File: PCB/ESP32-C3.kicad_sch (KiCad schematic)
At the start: 41 parts, among them J1 BattConn+, J2 BattConn-, SW1 TAK_6mm_THT, U1 USB-C-16P-SMD, U2 XT4052K421MR-G, U3 ESP32-C3, U4 RS3236-3.3YF5, X1 DPS_I2C, Y1 40MHz_S3240000151040

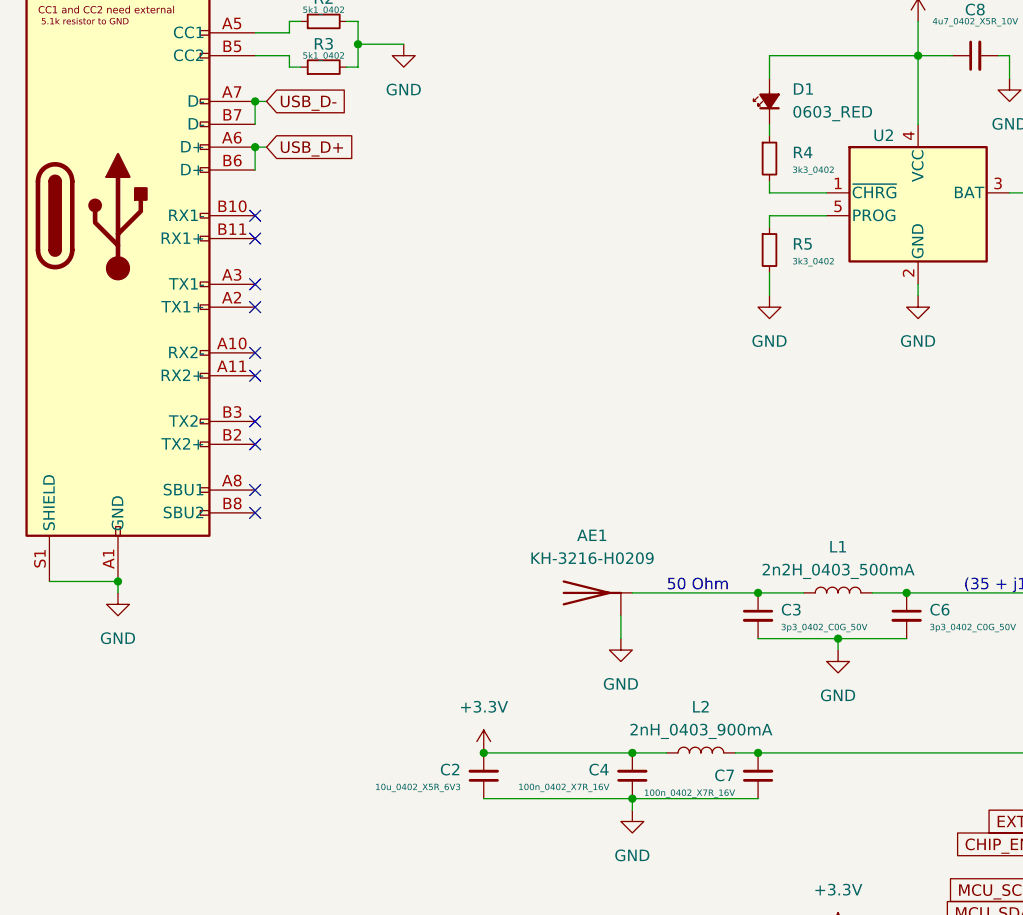
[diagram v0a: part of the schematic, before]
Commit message: update to KiCad 7
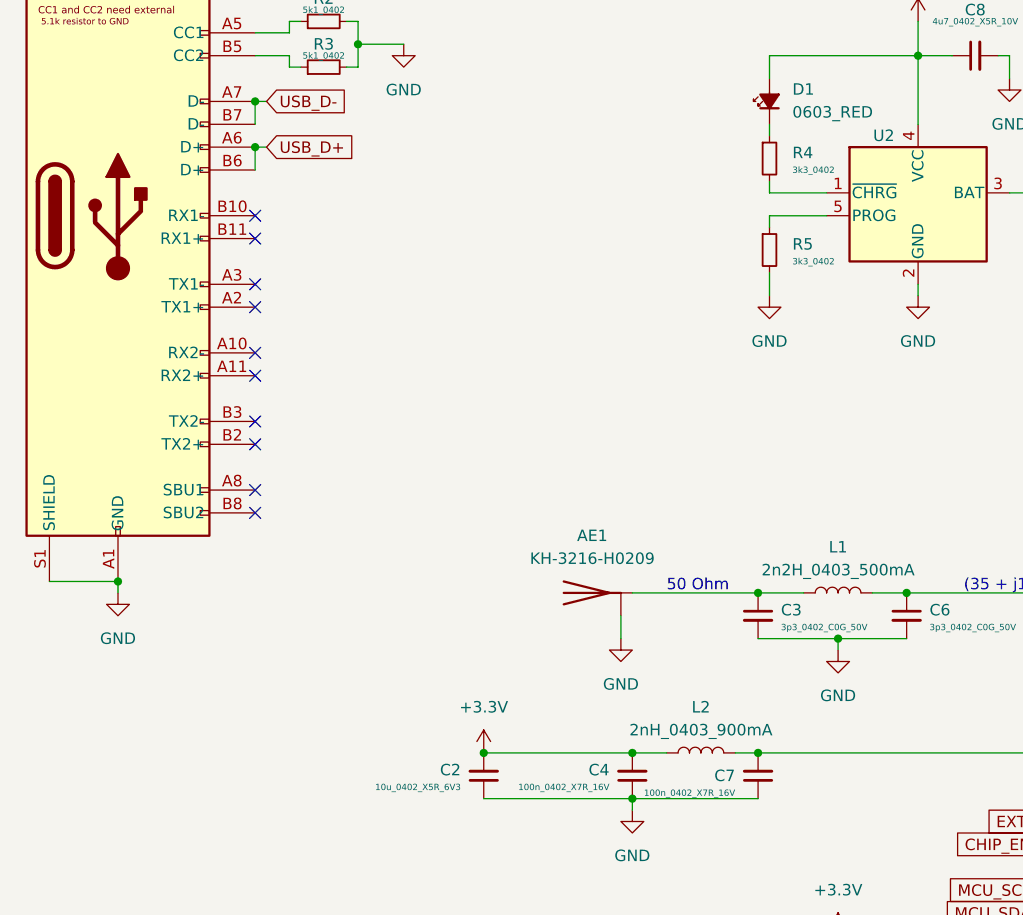
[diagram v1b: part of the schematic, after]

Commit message: updated the charging circuit
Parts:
- removed C10, C18: 1u_0402_X5R_25V, Capacitor_SMD:C_0402_1005Metric, symbol capacitor_smd_standard:1u_0402_X5R_25V
- removed C13: 10n_0402_X7R_50V, Capacitor_SMD:C_0402_1005Metric, symbol capacitor_smd_standard:10n_0402_X7R_50V
- removed C8: 4u7_0402_X5R_10V, Capacitor_SMD:C_0402_1005Metric, symbol ESP32-C3_Bib:4u7_0402_X5R_10V
- removed C9: 10u_0402_X5R_6V3, Capacitor_SMD:C_0402_1005Metric, symbol capacitor_smd_standard:10u_0402_X5R_6V3
- removed D1: 0603_RED, LED_SMD:LED_0603_1608Metric, symbol led:0603_RED
- removed D2, D3: 1N5819WS(Basic), Diode_SMD:D_SOD-323_HandSoldering, symbol 1_diodes:1N5819WS(Basic)
- removed J1: BattConn+, Connector_PinSocket_2.54mm:PinSocket_1x01_P2.54mm_Vertical, symbol Connector_Generic:Conn_01x01
- removed J2: BattConn-, Connector_PinSocket_2.54mm:PinSocket_1x01_P2.54mm_Vertical, symbol Connector_Generic:Conn_01x01
- removed R4, R5: 3k3_0402, Resistor_SMD:R_0402_1005Metric, symbol resistor_smd_standard:3k3_0402
- removed SW1: TAK_6mm_THT, Button_Switch_THT:SW_PUSH_6mm_H5mm, symbol 1_switch:TAK_6mm_THT
- removed U2: XT4052K421MR-G, Package_TO_SOT_SMD:TSOT-23-5, symbol ESP32-C3_Bib:XT4052K421MR-G
- removed U4: RS3236-3.3YF5, Package_TO_SOT_SMD:SOT-23-5, symbol ESP32-C3_Bib:RS3236-3.3YF5
- added SW2: TS4535TP 250gf 009, switch:SW_SPST_TL3305B, symbol 1_switch:TS4535TP 250gf 009
- added TP1: BAT+, testpoints:TP3, symbol 0_testpoints:TP_3CH
- added TP2: BAT-, testpoints:TP3, symbol 0_testpoints:TP_3CH
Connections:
- net +BATT: now also TP1.1
- net EXTI: now also SW2.2
- net GND: now also SW2.1, TP2.1
- net GPIO8: now reaches U3.14 (GPIO8)
- no-connect marks 27 -> 26
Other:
- added sheet charger (charger.kicad_sch)
- note removed: "Charching Current: V_prog = 1V, R_prog=3.3k 303mA = (V_prog / R_prog) * 1000"

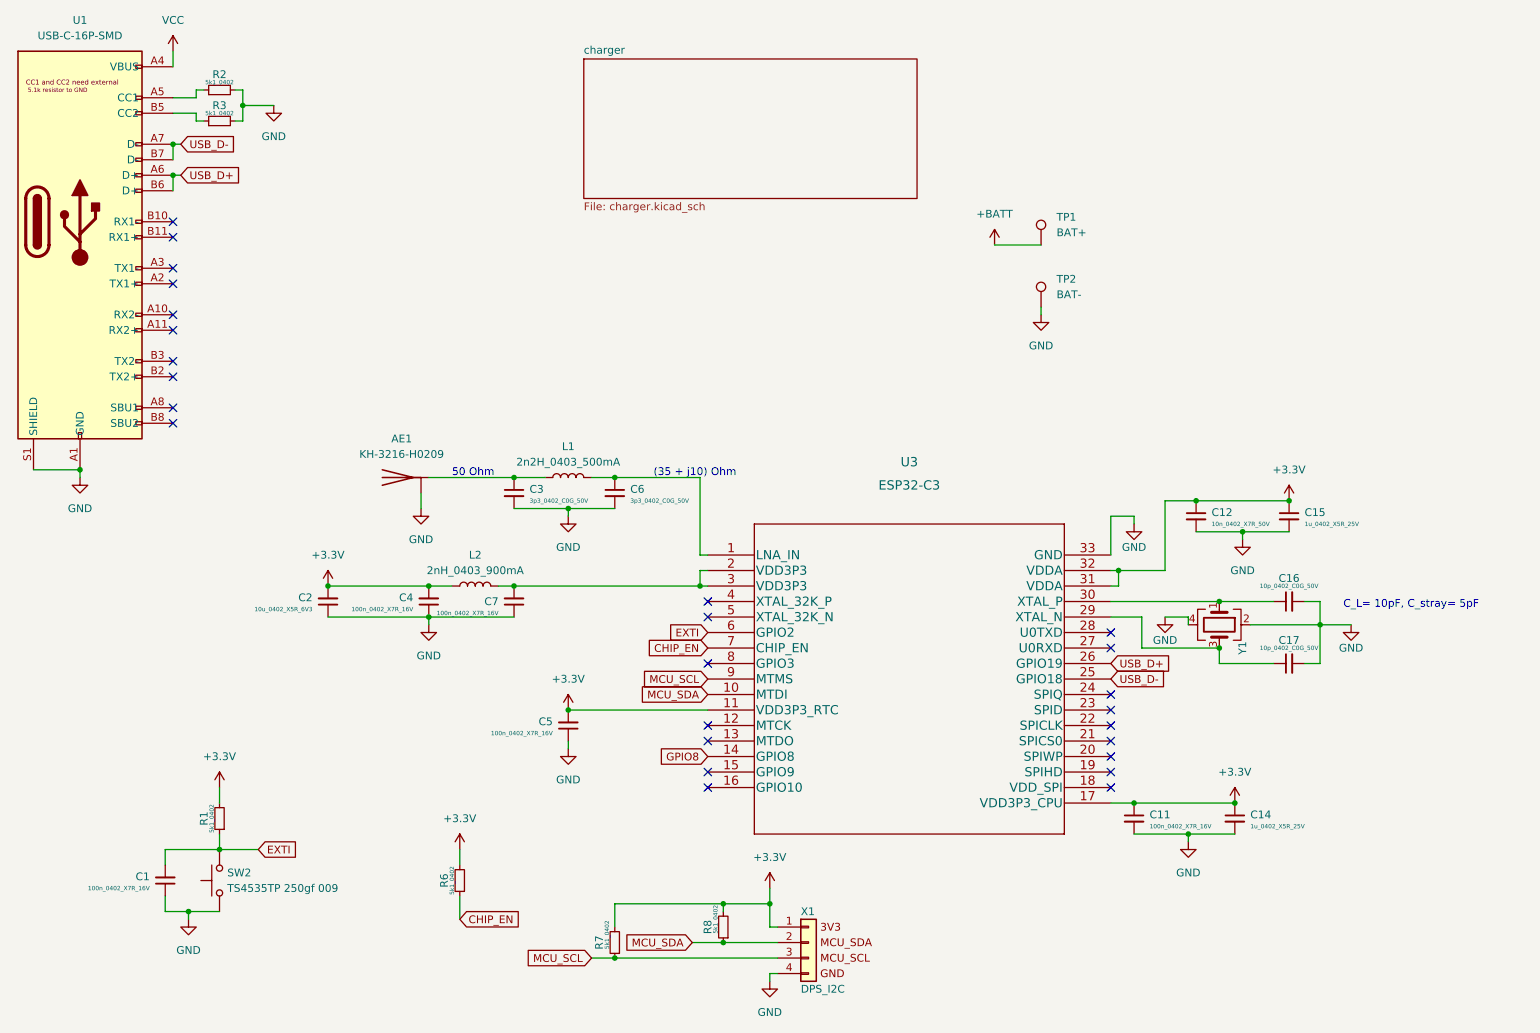
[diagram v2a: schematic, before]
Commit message: Mit dem Layout angefangen
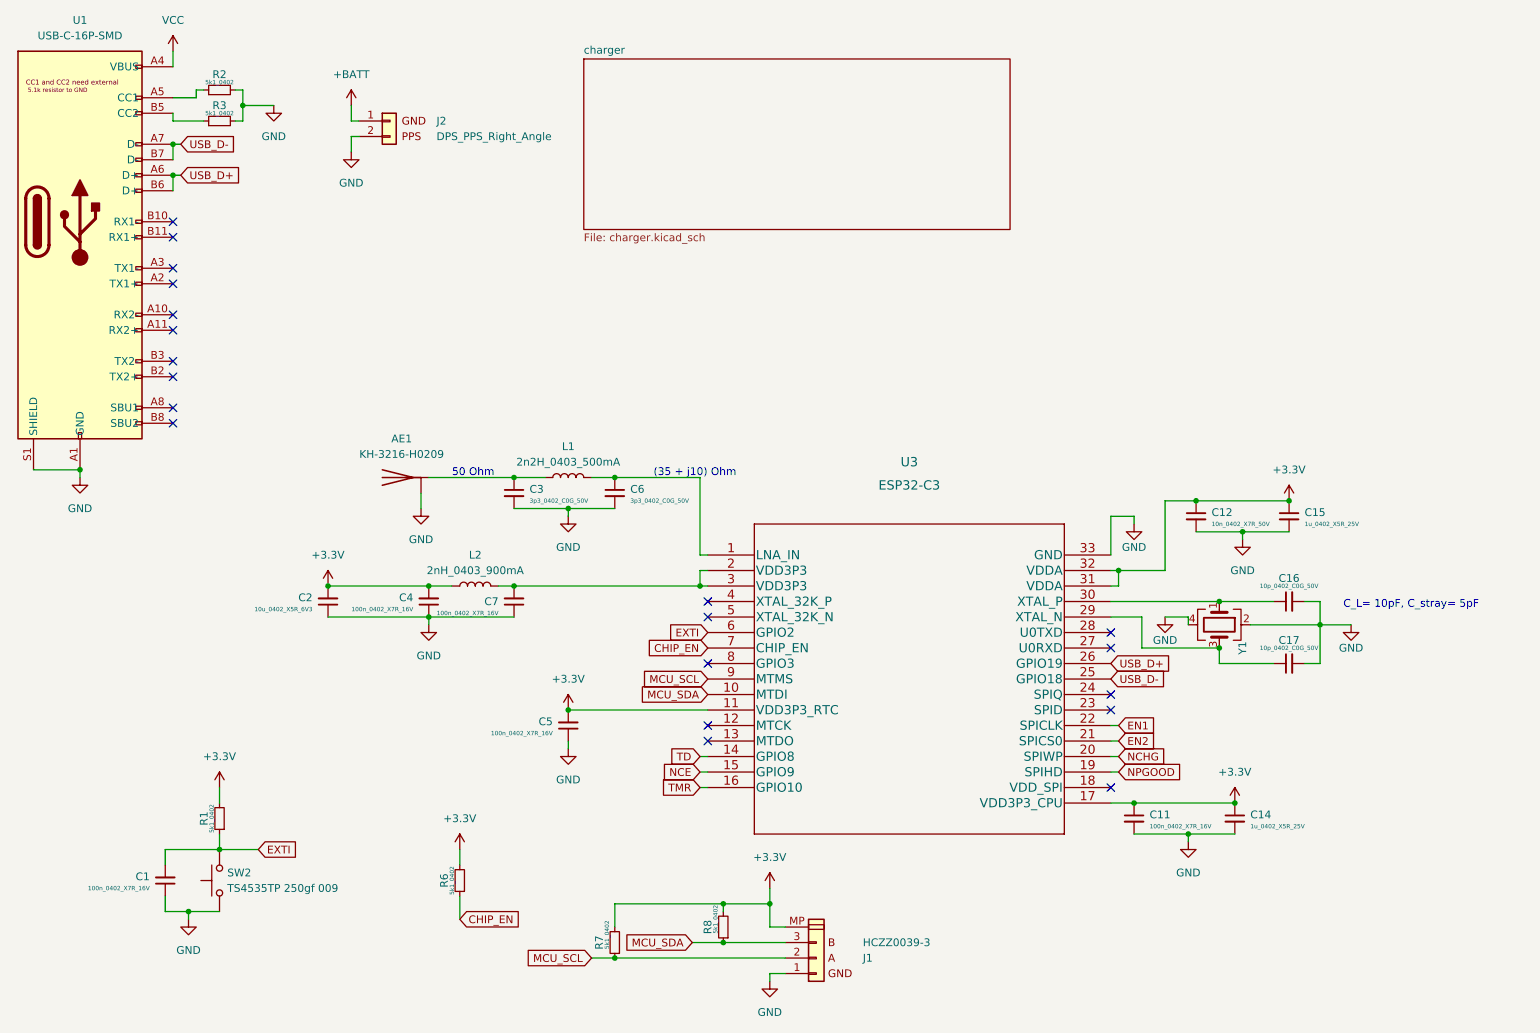
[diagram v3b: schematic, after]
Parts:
- removed TP1: BAT+, testpoints:TP3, symbol 0_testpoints:TP_3CH
- removed TP2: BAT-, testpoints:TP3, symbol 0_testpoints:TP_3CH
- removed X1: DPS_I2C, Connector_JST:JST_PH_B4B-PH-K_1x04_P2.00mm_Vertical, symbol DPS_connectors:DPS_I2C
- added J1: HCZZ0039-3, Connector_JST:JST_SH_SM03B-SRSS-TB_1x03-1MP_P1.00mm_Horizontal, symbol DPS_connectors:DPS_485
- added J2: DPS_PPS_Right_Angle, Connector_JST:JST_PH_S2B-PH-K_1x02_P2.00mm_Horizontal, symbol DPS_connectors:DPS_PPS_Right_Angle
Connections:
- net +3.3V: now also J1.MP
- net +BATT: now also J2.1 (Pin_1)
- net GND: now also J1.1 (Pin_1), J2.2 (Pin_2)
- net MCU_SCL: now also J1.2 (Pin_2)
- net MCU_SDA: now also J1.3 (Pin_3)
- net NCE: now reaches U3.15 (GPIO9)
- net TMR: now reaches U3.16 (GPIO10)
- net NPGOOD: now reaches U3.19 (SPIHD)
- net NCHG: now reaches U3.20 (SPIWP)
- net EN2: now reaches U3.21 (SPICS0)
- net EN1: now reaches U3.22 (SPICLK)
- net GPIO8 renamed TD
- no-connect marks 26 -> 20

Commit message: Layout weiter gemacht.
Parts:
- C1, C11, C4, C5, C7: QtyReel (none) -> 10000
- U1: Partnumber (none) -> SOFNG MC-311D
- U3: footprint ESP32-C3:ESP32-C3 -> Package_DFN_QFN:QFN-32-1EP_5x5mm_P0.5mm_EP3.7x3.7mm
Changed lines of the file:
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@@
       (effects (font (size 1.27 1.27)))
     )
-    (property "Value" "10p_0402_C0G_50V" (at 228.6 110.49 90)
-      (effects (font (size 0.7 0.7)))
+    (property "Value" "10p_0402_C0G_50V" (at 230.632 112.776 0)
+      (effects (font (size 0.7 0.7)) (justify left))
     )
     (property "Footprint" "Capacitor_SMD:C_0402_1005Metric" (at 228.6 113.03 0)
@@
   (symbol (lib_id "capacitor_smd_standard:100n_0402_X7R_16V") (at 87.63 113.03 0) (mirror x) (unit 1)
     (in_bom yes) (on_board yes) (dnp no) (fields_autoplaced)
-    (property "Reference" "C4" (at 85.09 112.3885 0)
+    (property "Reference" "C4" (at 85.09 112.3886 0)
       (effects (font (size 1.27 1.27)) (justify right))
     )
@@
       (effects (font (size 1.27 1.27)) hide)
     )
+    (property "QtyReel" "10000" (at 87.63 113.03 0)
+      (effects (font (size 1.27 1.27)) hide)
+    )
     (pin "1")
     (pin "2")
@@
   (symbol (lib_id "capacitor_smd_standard:10u_0402_X5R_6V3") (at 71.12 113.03 0) (mirror x) (unit 1)
     (in_bom yes) (on_board yes) (dnp no) (fields_autoplaced)
-    (property "Reference" "C2" (at 68.58 112.3885 0)
+    (property "Reference" "C2" (at 68.58 112.3886 0)
       (effects (font (size 1.27 1.27)) (justify right))
     )
@@
       (effects (font (size 1.27 1.27)))
     )
-    (property "Value" "5k1_0402" (at 116.84 167.64 90)
-      (effects (font (size 0.7 0.7)))
+    (property "Value" "5k1_0402" (at 116.84 168.91 0)
+      (effects (font (size 0.7 0.7)) (justify left))
     )
     (property "Footprint" "Resistor_SMD:R_0402_1005Metric" (at 134.62 157.48 0)
@@
   (symbol (lib_id "capacitor_smd_standard:1u_0402_X5R_25V") (at 219.71 148.59 0) (unit 1)
     (in_bom yes) (on_board yes) (dnp no) (fields_autoplaced)
-    (property "Reference" "C14" (at 222.25 147.9612 0)
+    (property "Reference" "C14" (at 222.25 147.9613 0)
       (effects (font (size 1.27 1.27)) (justify left))
     )
@@
       (effects (font (size 1.27 1.27)))
     )
-    (property "Value" "2nH_0403_900mA" (at 95.25 107.95 90)
+    (property "Value" "2nH_0403_900mA" (at 95.25 108.585 90)
       (effects (font (size 1.27 1.27)))
     )
@@
       (effects (font (size 1.27 1.27)))
     )
-    (property "Value" "2n2H_0403_500mA" (at 110.49 90.17 90)
+    (property "Value" "2n2H_0403_500mA" (at 110.49 90.805 90)
       (effects (font (size 1.27 1.27)))
     )
@@
       (effects (font (size 1.27 1.27)))
     )
-    (property "Value" "5k1_0402" (at 134.62 165.1 90)
-      (effects (font (size 0.7 0.7)))
+    (property "Value" "5k1_0402" (at 134.62 166.37 0)
+      (effects (font (size 0.7 0.7)) (justify left))
     )
     (property "Footprint" "Resistor_SMD:R_0402_1005Metric" (at 152.4 154.94 0)
@@
       (effects (font (size 1.27 1.27)))
     )
-    (property "Value" "10p_0402_C0G_50V" (at 228.6 120.65 90)
-      (effects (font (size 0.7 0.7)))
+    (property "Value" "10p_0402_C0G_50V" (at 230.632 122.936 0)
+      (effects (font (size 0.7 0.7)) (justify left))
     )
     (property "Footprint" "Capacitor_SMD:C_0402_1005Metric" (at 228.6 123.19 0)
@@
       (effects (font (size 1.27 1.27)))
     )
-    (property "Value" "5k1_0402" (at 53.34 33.02 90)
-      (effects (font (size 0.7 0.7)))
+    (property "Value" "5k1_0402" (at 53.34 33.02 0)
+      (effects (font (size 0.7 0.7)) (justify left))
     )
     (property "Footprint" "Resistor_SMD:R_0402_1005Metric" (at 64.77 50.8 0)
@@
       (effects (font (size 1.27 1.27)))
     )
-    (property "Value" "5k1_0402" (at 91.44 158.75 90)
-      (effects (font (size 0.7 0.7)))
+    (property "Value" "5k1_0402" (at 91.44 158.75 0)
+      (effects (font (size 0.7 0.7)) (justify left))
     )
     (property "Footprint" "Resistor_SMD:R_0402_1005Metric" (at 109.22 147.32 0)
@@
       (effects (font (size 1.27 1.27)))
     )
-    (property "Value" "5k1_0402" (at 52.07 148.59 90)
-      (effects (font (size 0.7 0.7)))
+    (property "Value" "5k1_0402" (at 52.07 148.59 0)
+      (effects (font (size 0.7 0.7)) (justify left))
     )
     (property "Footprint" "Resistor_SMD:R_0402_1005Metric" (at 69.85 137.16 0)
@@
   (symbol (lib_id "capacitor_smd_standard:100n_0402_X7R_16V") (at 203.2 148.59 0) (unit 1)
     (in_bom yes) (on_board yes) (dnp no) (fields_autoplaced)
-    (property "Reference" "C11" (at 205.74 147.9612 0)
+    (property "Reference" "C11" (at 205.74 147.9613 0)
       (effects (font (size 1.27 1.27)) (justify left))
     )
@@
     )
     (property "Price1000" "0.0006" (at 203.2 148.59 0)
+      (effects (font (size 1.27 1.27)) hide)
+    )
+    (property "QtyReel" "10000" (at 203.2 148.59 0)
       (effects (font (size 1.27 1.27)) hide)
     )
@@
   (symbol (lib_id "ESP32-C3_Bib:3p3_0402_C0G_50V") (at 101.6 95.25 0) (unit 1)
     (in_bom yes) (on_board yes) (dnp no) (fields_autoplaced)
-    (property "Reference" "C3" (at 104.14 94.6212 0)
+    (property "Reference" "C3" (at 104.14 94.6213 0)
       (effects (font (size 1.27 1.27)) (justify left))
     )
@@
       (effects (font (size 1.27 1.27)))
     )
-    (property "Value" "40MHz_S3240000151040" (at 218.2114 133.35 0)
-      (effects (font (size 1.27 1.27)) hide)
+    (property "Value" "40MHz_S3240000151040" (at 220.345 120.015 0)
+      (effects (font (size 1.27 1.27)) (justify left))
     )
     (property "Footprint" "Crystal:Crystal_SMD_3225-4Pin_3.2x2.5mm" (at 217.17 116.84 0)
@@
   (symbol (lib_id "ESP32-C3_Bib:3p3_0402_C0G_50V") (at 118.11 95.25 0) (unit 1)
     (in_bom yes) (on_board yes) (dnp no) (fields_autoplaced)
-    (property "Reference" "C6" (at 120.65 94.6212 0)
+    (property "Reference" "C6" (at 120.65 94.6213 0)
       (effects (font (size 1.27 1.27)) (justify left))
     )
@@
       (effects (font (size 1.27 1.27)))
     )
-    (property "Value" "5k1_0402" (at 53.34 27.94 90)
-      (effects (font (size 0.7 0.7)))
+    (property "Value" "5k1_0402" (at 53.34 27.94 0)
+      (effects (font (size 0.7 0.7)) (justify left))
     )
     (property "Footprint" "Resistor_SMD:R_0402_1005Metric" (at 64.77 45.72 0)
@@
   (symbol (lib_id "capacitor_smd_standard:1u_0402_X5R_25V") (at 228.6 99.06 0) (unit 1)
     (in_bom yes) (on_board yes) (dnp no) (fields_autoplaced)
-    (property "Reference" "C15" (at 231.14 98.4312 0)
+    (property "Reference" "C15" (at 231.14 98.4313 0)
       (effects (font (size 1.27 1.27)) (justify left))
     )
@@
       (effects (font (size 1.27 1.27)) (justify left))
     )
-    (property "Value" "HCZZ0039-3" (at 158.75 168.91 0)
-      (effects (font (size 1.27 1.27)) (justify left))
+    (property "Value" "HCZZ0039-3" (at 161.29 165.1 0)
+      (effects (font (size 1.27 1.27)))
     )
     (property "Footprint" "Connector_JST:JST_SH_SM03B-SRSS-TB_1x03-1MP_P1.00mm_Horizontal" (at 150.495 167.005 0)
@@
   (symbol (lib_id "capacitor_smd_standard:10n_0402_X7R_50V") (at 213.36 99.06 0) (unit 1)
     (in_bom yes) (on_board yes) (dnp no) (fields_autoplaced)
-    (property "Reference" "C12" (at 215.9 98.4312 0)
+    (property "Reference" "C12" (at 215.9 98.4313 0)
       (effects (font (size 1.27 1.27)) (justify left))
     )
@@
     )
     (property "Description" "1 12 Female Type-C SMD USB Connectors ROHS " (at 30.48 55.88 0)
+      (effects (font (size 1.27 1.27)) hide)
+    )
+    (property "Partnumber" "SOFNG MC-311D" (at 30.48 55.88 0)
       (effects (font (size 1.27 1.27)) hide)
     )
@@
   (symbol (lib_id "capacitor_smd_standard:100n_0402_X7R_16V") (at 110.49 133.35 0) (mirror x) (unit 1)
     (in_bom yes) (on_board yes) (dnp no) (fields_autoplaced)
-    (property "Reference" "C5" (at 107.95 132.7085 0)
+    (property "Reference" "C5" (at 107.95 132.7086 0)
       (effects (font (size 1.27 1.27)) (justify right))
     )
@@
     )
     (property "Price1000" "0.0006" (at 110.49 133.35 0)
+      (effects (font (size 1.27 1.27)) hide)
+    )
+    (property "QtyReel" "10000" (at 110.49 133.35 0)
       (effects (font (size 1.27 1.27)) hide)
     )
@@
       (effects (font (size 1.27 1.27)) (justify right))
     )
-    (property "Value" "100n_0402_X7R_16V" (at 99.06 114.9351 0)
-      (effects (font (size 0.7 0.7)) (justify right))
+    (property "Value" "100n_0402_X7R_16V" (at 101.854 110.998 0)
+      (effects (font (size 0.7 0.7)) (justify left))
     )
     (property "Footprint" "Capacitor_SMD:C_0402_1005Metric" (at 101.6 113.03 0)
@@
       (effects (font (size 1.27 1.27)) hide)
     )
+    (property "QtyReel" "10000" (at 101.6 113.03 0)
+      (effects (font (size 1.27 1.27)) hide)
+    )
     (pin "1")
     (pin "2")
@@
   (symbol (lib_id "capacitor_smd_standard:100n_0402_X7R_16V") (at 44.45 158.75 0) (mirror x) (unit 1)
     (in_bom yes) (on_board yes) (dnp no) (fields_autoplaced)
-    (property "Reference" "C1" (at 41.91 158.1085 0)
+    (property "Reference" "C1" (at 41.91 158.1086 0)
       (effects (font (size 1.27 1.27)) (justify right))
     )
@@
       (effects (font (size 1.27 1.27)) hide)
     )
+    (property "QtyReel" "10000" (at 44.45 158.75 0)
+      (effects (font (size 1.27 1.27)) hide)
+    )
     (pin "1")
     (pin "2")
@@
       (effects (font (size 1.524 1.524)))
     )
-    (property "Footprint" "ESP32-C3:ESP32-C3" (at 166.37 97.79 0)
+    (property "Footprint" "Package_DFN_QFN:QFN-32-1EP_5x5mm_P0.5mm_EP3.7x3.7mm" (at 166.37 97.79 0)
       (effects (font (size 1.524 1.524)) hide)
     )
